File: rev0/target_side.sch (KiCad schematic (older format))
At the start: 9 parts, among them IC1 ECP5-BGA256, U9 USB3343

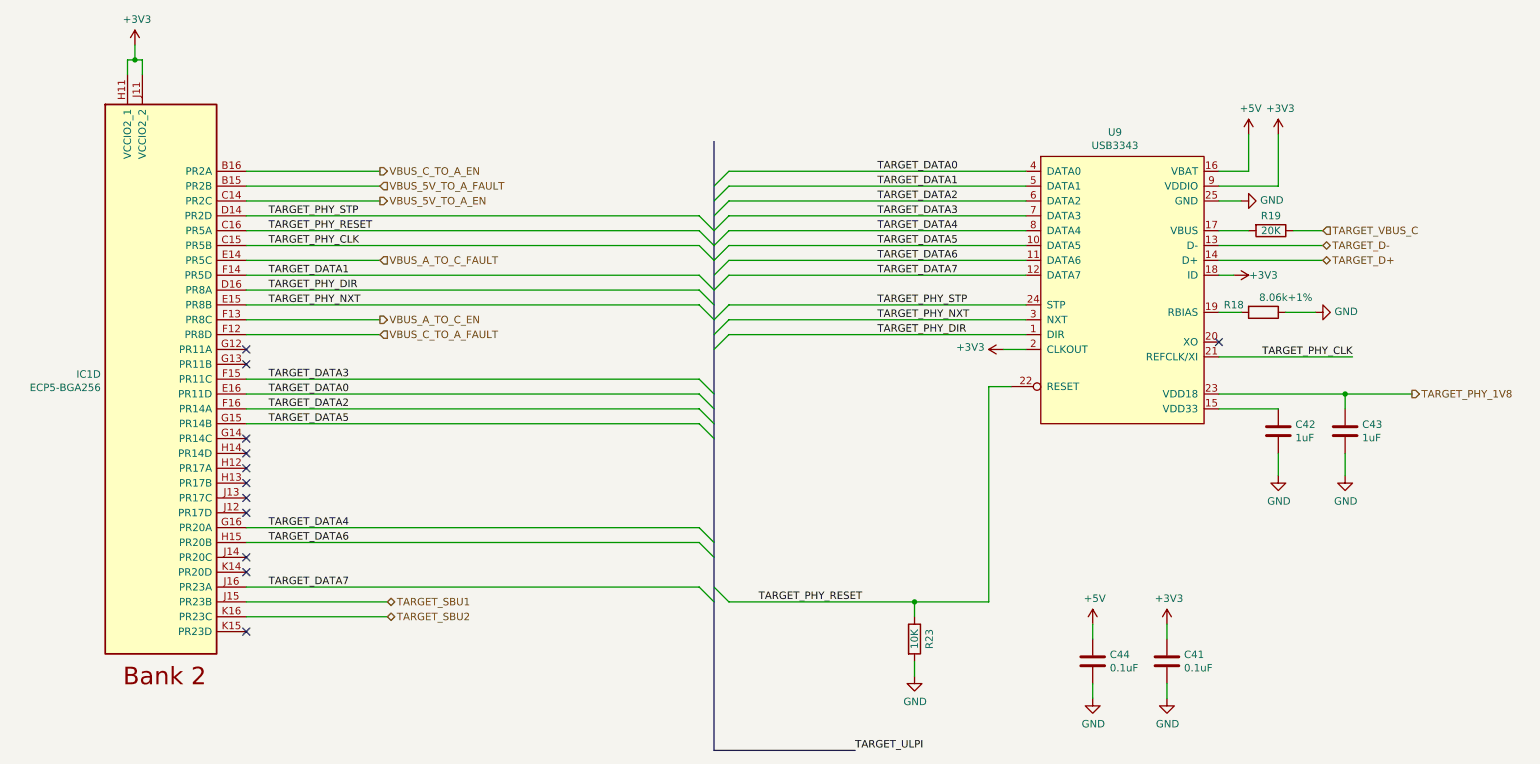
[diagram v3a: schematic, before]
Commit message: hardware: add more test points
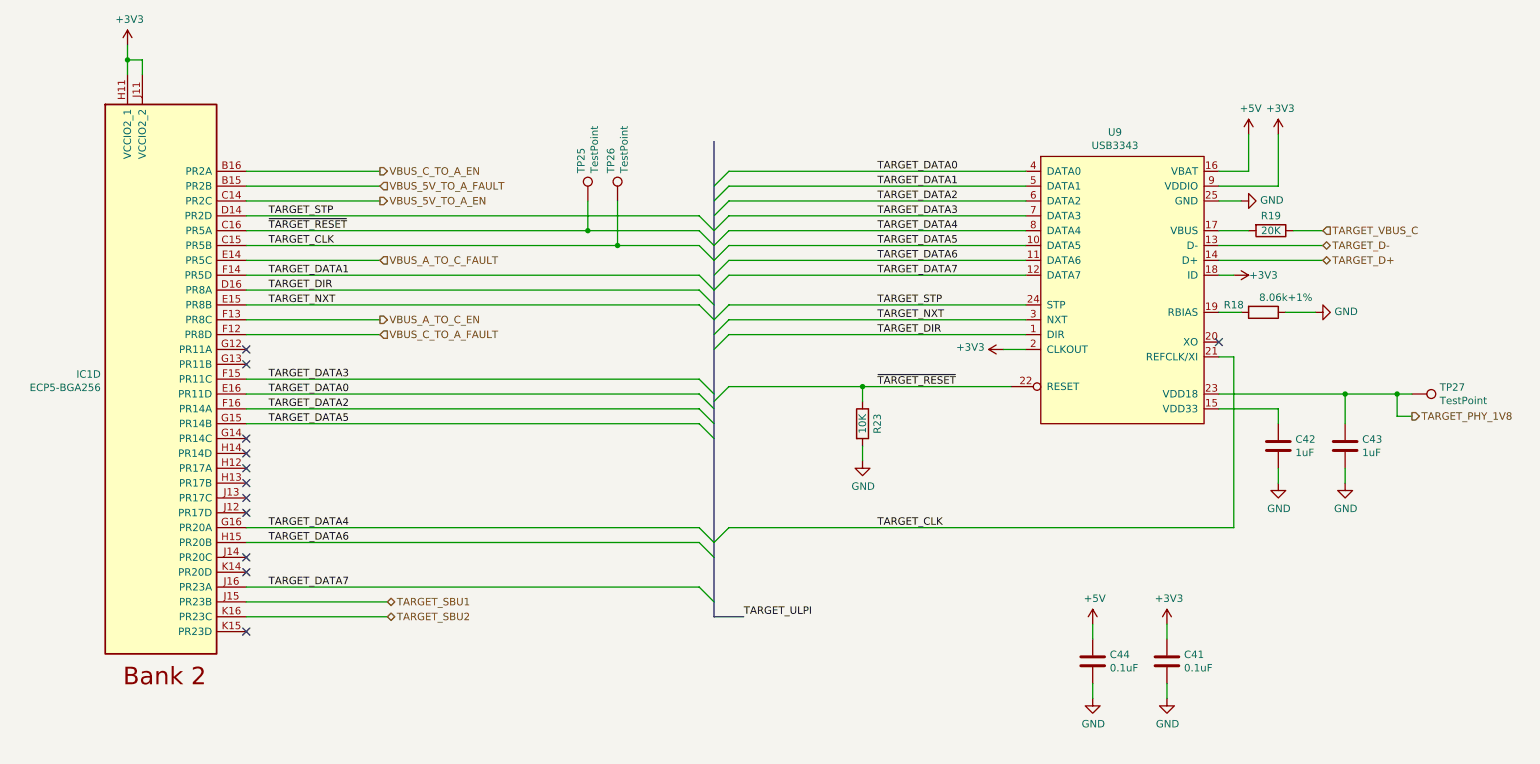
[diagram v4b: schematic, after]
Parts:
- added TP25, TP26, TP27: TestPoint, TestPoint:TestPoint_Pad_D1.0mm, symbol Connector:TestPoint
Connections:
- net TARGET_PHY_1V8: now also TP27.1
- net TARGET_PHY_CLK renamed TARGET_CLK
- net TARGET_CLK: now also TP26.1
- net TARGET_PHY_DIR renamed TARGET_DIR
- net TARGET_PHY_NXT renamed TARGET_NXT
- net TARGET_PHY_RESET renamed ~TARGET_RESET
- net ~TARGET_RESET: now also TP25.1
- net TARGET_PHY_STP renamed TARGET_STP
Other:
- moved on the sheet: C42, C43, R23

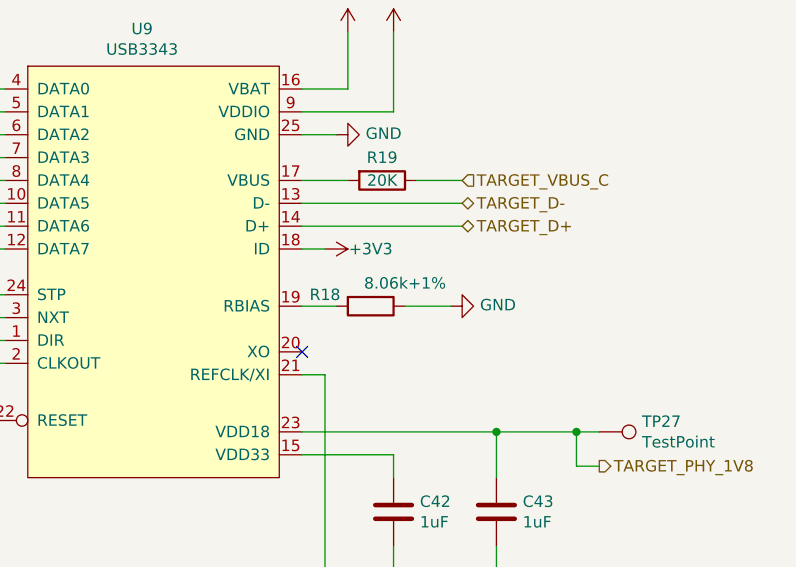
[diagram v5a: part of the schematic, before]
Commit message: hardware: select LEDs and series resistors
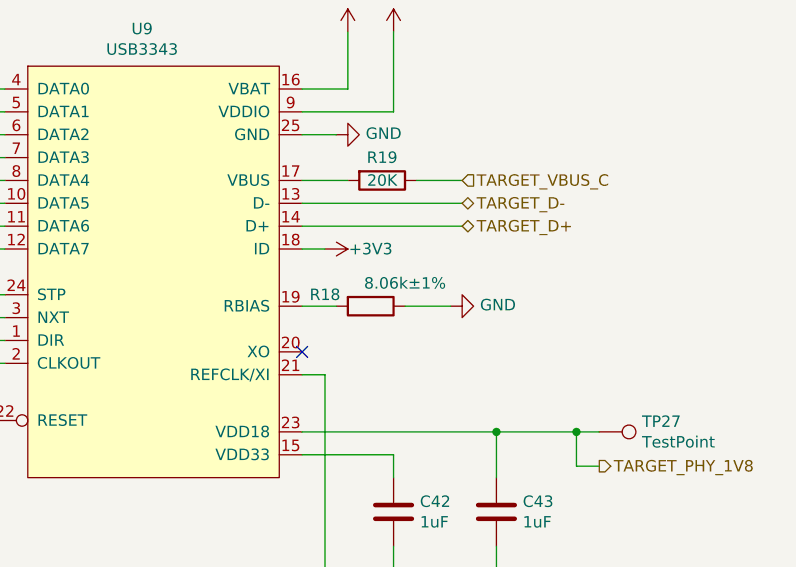
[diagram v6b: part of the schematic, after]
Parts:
- R18: value 8.06k+1% -> 8.06k±1%
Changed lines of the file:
@@
 Sheet 5 9
 Title "LUNA: Downstream / Target / Analysis Section"
-Date "2021-01-08"
+Date "2021-01-10"
 Rev "r0"
 Comp "Copyright 2019-2021 Great Scott Gadgets"
@@
 AR Path="/60B354AE/5DDE2B06" Ref="R39"  Part="1"
 F 0 "R18" V 9150 2850 50  0000 C CNN
-F 1 "8.06k+1%" V 9100 3200 50  0000 C CNN
+F 1 "8.06k±1%" V 9100 3200 50  0000 C CNN
 F 2 "Resistor_SMD:R_0402_1005Metric" V 9130 3050 50  0001 C CNN
 F 3 "~" H 9200 3050 50  0001 C CNN
